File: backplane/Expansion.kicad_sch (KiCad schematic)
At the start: 27 parts, among them U401 74HC245, U402 74HC245, U403 74HC245, U404 74HC245, U405 74HC245, U406 74HC245, U407 ATF22V10C, U408 SY100EL14V

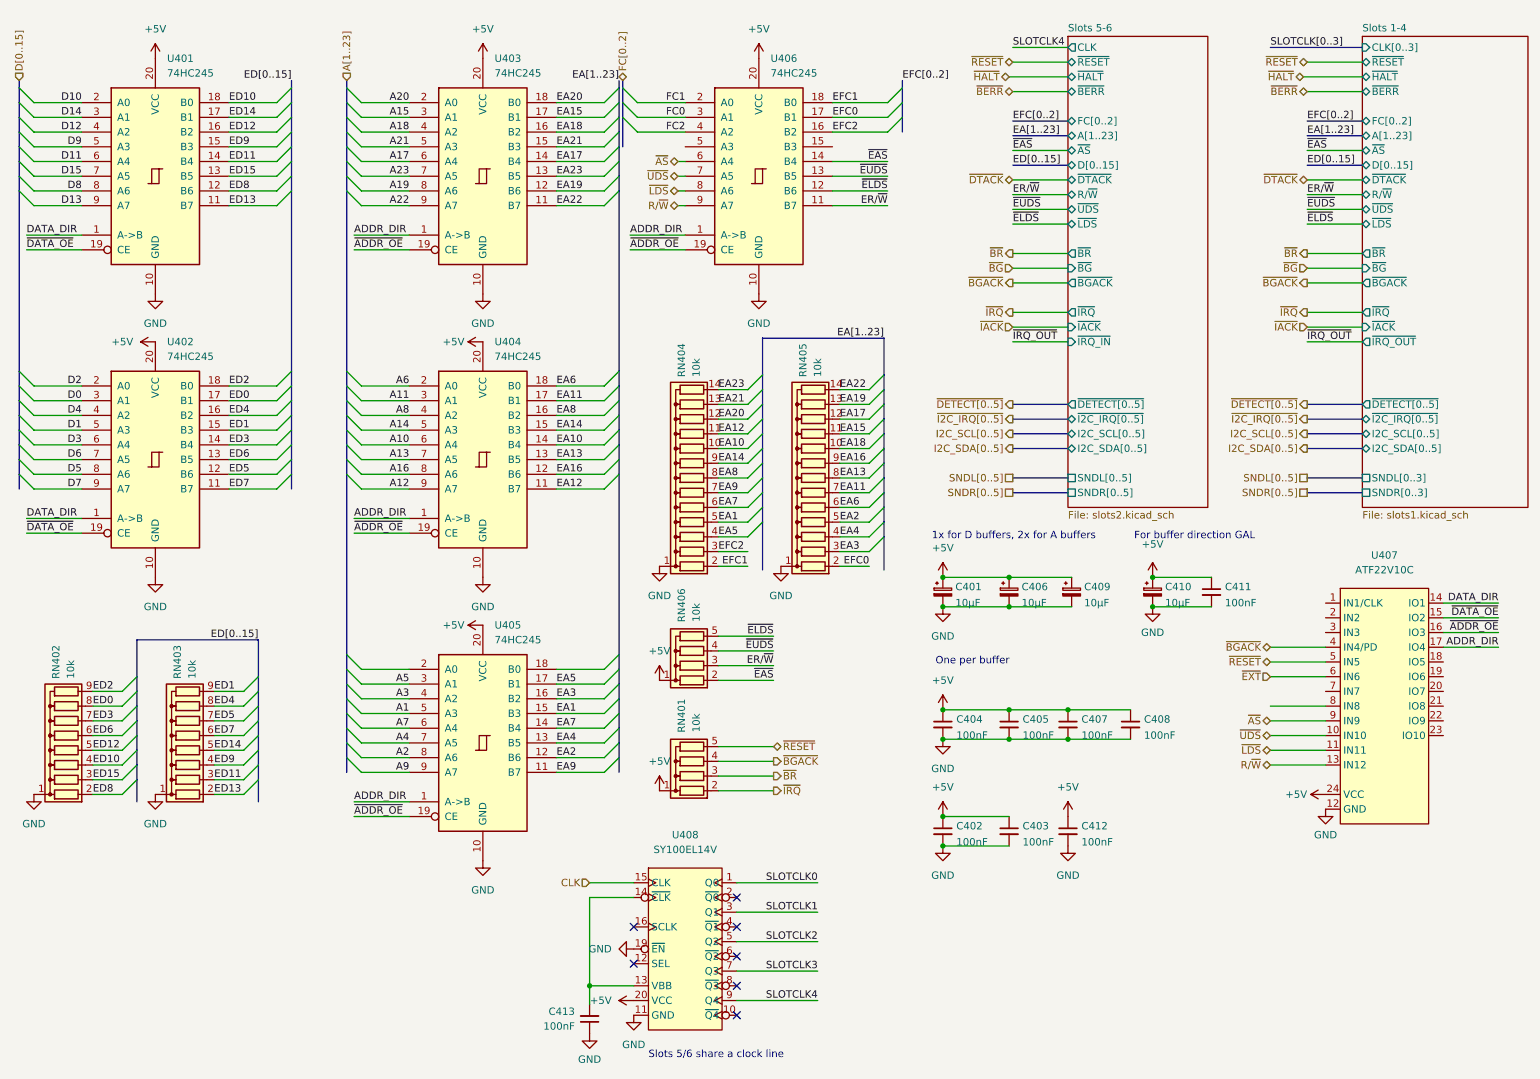
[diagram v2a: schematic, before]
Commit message: Backplane mechanical improvements
- Added screw holes to the backplane; they may or may not actually be
  correct but the spacing between them should be right. We've got holes
  every two HU's (2x .2") for extra spacing/material between holes

- Added reset LED and some more pull ups

- Minor tweaks to backplane management card
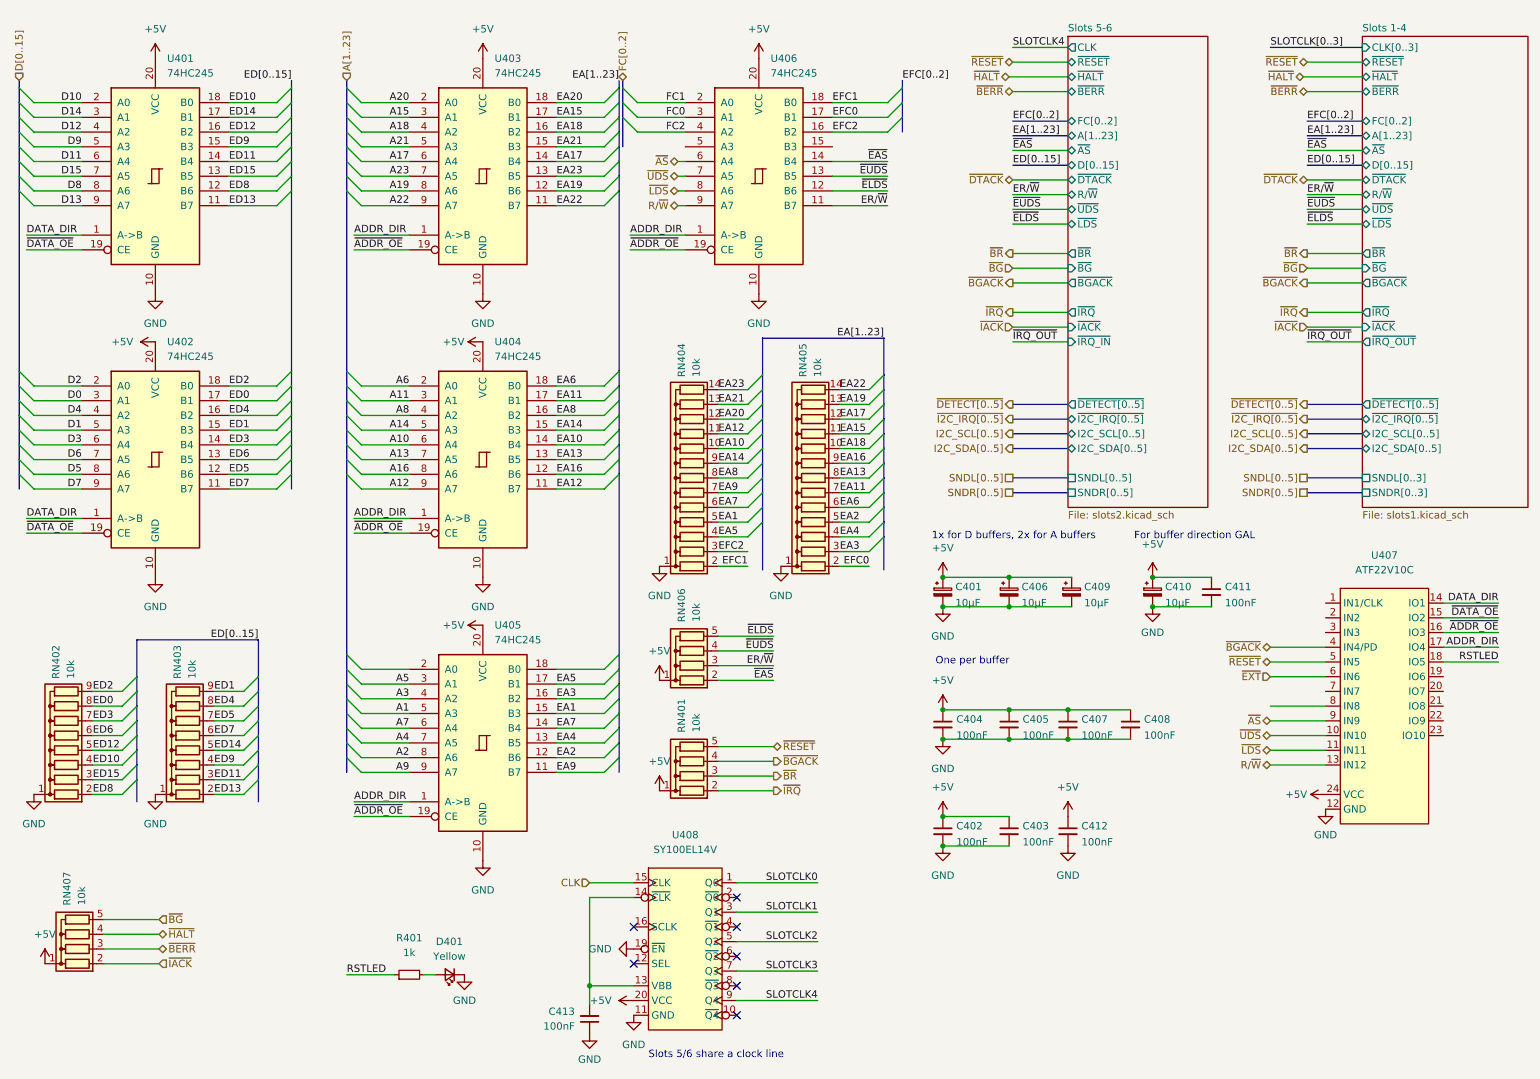
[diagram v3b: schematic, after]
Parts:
- added D401: Yellow, LED_SMD:LED_0805_2012Metric, symbol Device:LED_Small
- added R401: 1k, Resistor_SMD:R_0805_2012Metric, symbol Device:R_Small
- added RN407: 10k, Resistor_THT:R_Array_SIP5, symbol Device:R_Network04
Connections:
- net +5V: now also RN407.1 (common)
- net GND: now also D401.1 (K)
- net ~{BERR}: now also RN407.3 (R2)
- net ~{BG}: now also RN407.5 (R4)
- net ~{HALT}: now also RN407.4 (R3)
- net ~{IACK}: now also RN407.2 (R1)
- net RSTLED: now reaches U407.18 (IO5)
- net RSTLED: now also R401.1
- new net: D401.2 (A), R401.2
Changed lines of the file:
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@@
     (stroke (width 0) (type default) (color 0 0 0 0))
   )
+  (wire (pts (xy 265.43 127) (xy 274.955 127))
+    (stroke (width 0) (type default) (color 0 0 0 0))
+  )
   (wire (pts (xy 120.65 30.48) (xy 112.395 30.48))
     (stroke (width 0) (type default) (color 0 0 0 0))
@@
     (stroke (width 0) (type default) (color 0 0 0 0))
   )
+  (wire (pts (xy 34.29 176.53) (xy 43.815 176.53))
+    (stroke (width 0) (type default) (color 0 0 0 0))
+  )
   (bus (pts (xy 172.085 27.94) (xy 172.085 30.48))
     (stroke (width 0) (type default) (color 0 0 0 0))
@@
     (stroke (width 0) (type default) (color 0 0 0 0))
   )
+  (wire (pts (xy 34.29 179.07) (xy 43.815 179.07))
+    (stroke (width 0) (type default) (color 0 0 0 0))
+  )
   (bus (pts (xy 191.135 36.195) (xy 200.66 36.195))
     (stroke (width 0) (type default) (color 0 0 0 0))
@@
     (stroke (width 0) (type default) (color 0 0 0 0))
   )
+  (wire (pts (xy 34.29 171.45) (xy 43.815 171.45))
+    (stroke (width 0) (type default) (color 0 0 0 0))
+  )
   (bus (pts (xy 241.935 41.275) (xy 251.46 41.275))
     (stroke (width 0) (type default) (color 0 0 0 0))
@@
     (stroke (width 0) (type default) (color 0 0 0 0))
   )
+  (wire (pts (xy 34.29 173.99) (xy 43.815 173.99))
+    (stroke (width 0) (type default) (color 0 0 0 0))
+  )
   (wire (pts (xy 118.11 182.88) (xy 118.11 186.055))
     (stroke (width 0) (type default) (color 0 0 0 0))
@@
     (stroke (width 0) (type default) (color 0 0 0 0))
   )
+  (wire (pts (xy 89.535 180.975) (xy 91.44 180.975))
+    (stroke (width 0) (type default) (color 0 0 0 0))
+  )
   (bus (pts (xy 66.675 35.56) (xy 66.675 38.1))
     (stroke (width 0) (type default) (color 0 0 0 0))
@@
     (stroke (width 0) (type default) (color 0 0 0 0))
   )
+  (wire (pts (xy 84.455 180.975) (xy 76.2 180.975))
+    (stroke (width 0) (type default) (color 0 0 0 0))
+  )
   (bus (pts (xy 147.955 85.09) (xy 147.955 87.63))
     (stroke (width 0) (type default) (color 0 0 0 0))
@@
     (effects (font (size 1.27 1.27)) (justify left bottom))
   )
+  (label "RSTLED" (at 274.955 127 180)
+    (effects (font (size 1.27 1.27)) (justify right bottom))
+  )
   (label "D11" (at 30.48 40.64 180)
     (effects (font (size 1.27 1.27)) (justify right bottom))
@@
     (effects (font (size 1.27 1.27)) (justify right bottom))
   )
+  (label "RSTLED" (at 76.2 180.975 0)
+    (effects (font (size 1.27 1.27)) (justify left bottom))
+  )
   (label "D7" (at 30.48 97.155 180)
     (effects (font (size 1.27 1.27)) (justify right bottom))
@@
     (effects (font (size 1.27 1.27)) (justify right))
   )
+  (hierarchical_label "~{HALT}" (shape bidirectional) (at 43.815 173.99 0)
+    (effects (font (size 1.27 1.27)) (justify left))
+  )
   (hierarchical_label "~{IRQ}" (shape output) (at 241.935 66.675 180)
     (effects (font (size 1.27 1.27)) (justify right))
@@
     (effects (font (size 1.27 1.27)) (justify left))
   )
+  (hierarchical_label "~{IACK}" (shape input) (at 43.815 179.07 0)
+    (effects (font (size 1.27 1.27)) (justify left))
+  )
   (hierarchical_label "~{BG}" (shape input) (at 241.935 59.055 180)
     (effects (font (size 1.27 1.27)) (justify right))
@@
     (effects (font (size 1.27 1.27)) (justify right))
   )
+  (hierarchical_label "~{BG}" (shape input) (at 43.815 171.45 0)
+    (effects (font (size 1.27 1.27)) (justify left))
+  )
   (hierarchical_label "~{DTACK}" (shape bidirectional) (at 241.935 43.815 180)
     (effects (font (size 1.27 1.27)) (justify right))
@@
     (effects (font (size 1.27 1.27)) (justify right))
   )
+  (hierarchical_label "~{BERR}" (shape bidirectional) (at 43.815 176.53 0)
+    (effects (font (size 1.27 1.27)) (justify left))
+  )
   (hierarchical_label "~{RESET}" (shape bidirectional) (at 241.935 23.495 180)
     (effects (font (size 1.27 1.27)) (justify right))
@@
     (pin "2")
   )
+  (symbol (lib_id "Device:R_Network04") (at 29.21 173.99 90) (unit 1)
+    (in_bom yes) (on_board yes)
+    (property "Reference" "RN407" (id 0) (at 27.94 163.195 0)
+      (effects (font (size 1.27 1.27)) (justify right))
+    )
+    (property "Value" "10k" (id 1) (at 30.48 165.735 0)
+      (effects (font (size 1.27 1.27)) (justify right))
+    )
+    (property "Footprint" "Resistor_THT:R_Array_SIP5" (id 2) (at 29.21 167.005 90)
+      (effects (font (size 1.27 1.27)) hide)
+    )
+    (property "Datasheet" "http://www.vishay.com/docs/31509/csc.pdf" (id 3) (at 29.21 173.99 0)
+      (effects (font (size 1.27 1.27)) hide)
+    )
+    (property "MPN" "4605X-101-103LF" (id 4) (at 29.21 173.99 90)
+      (effects (font (size 1.27 1.27)) hide)
+    )
+    (pin "1")
+    (pin "2")
+    (pin "3")
+    (pin "4")
+    (pin "5")
+  )
   (symbol (lib_id "Device:C_Small") (at 190.5 137.795 0) (unit 1)
     (in_bom yes) (on_board yes) (fields_autoplaced)
@@
     (pin "1")
   )
+  (symbol (lib_id "power:+5V") (at 24.13 179.07 0) (unit 1)
+    (in_bom yes) (on_board yes) (fields_autoplaced)
+    (property "Reference" "#PWR0430" (id 0) (at 24.13 182.88 0)
+      (effects (font (size 1.27 1.27)) hide)
+    )
+    (property "Value" "+5V" (id 1) (at 24.13 173.99 0))
+    (property "Footprint" "" (id 2) (at 24.13 179.07 0)
+      (effects (font (size 1.27 1.27)) hide)
+    )
+    (property "Datasheet" "" (id 3) (at 24.13 179.07 0)
+      (effects (font (size 1.27 1.27)) hide)
+    )
+    (pin "1")
+  )
   (symbol (lib_id "power:+5V") (at 125.73 185.42 90) (unit 1)
     (in_bom yes) (on_board yes) (fields_autoplaced)
@@
     (pin "1")
   )
+  (symbol (lib_id "Device:R_Small") (at 86.995 180.975 90) (unit 1)
+    (in_bom yes) (on_board yes) (fields_autoplaced)
+    (property "Reference" "R401" (id 0) (at 86.995 174.625 90))
+    (property "Value" "1k" (id 1) (at 86.995 177.165 90))
+    (property "Footprint" "Resistor_SMD:R_0805_2012Metric" (id 2) (at 86.995 180.975 0)
+      (effects (font (size 1.27 1.27)) hide)
+    )
+    (property "Datasheet" "~" (id 3) (at 86.995 180.975 0)
+      (effects (font (size 1.27 1.27)) hide)
+    )
+    (pin "1")
+    (pin "2")
+  )
+  (symbol (lib_id "power:GND") (at 96.52 180.975 0) (unit 1)
+    (in_bom yes) (on_board yes) (fields_autoplaced)
+    (property "Reference" "#PWR0130" (id 0) (at 96.52 187.325 0)
+      (effects (font (size 1.27 1.27)) hide)
+    )
+    (property "Value" "GND" (id 1) (at 96.52 185.42 0))
+    (property "Footprint" "" (id 2) (at 96.52 180.975 0)
+      (effects (font (size 1.27 1.27)) hide)
+    )
+    (property "Datasheet" "" (id 3) (at 96.52 180.975 0)
+      (effects (font (size 1.27 1.27)) hide)
+    )
+    (pin "1")
+  )
   (symbol (lib_id "74xx:74HC245") (at 147.32 43.18 0) (unit 1)
     (in_bom yes) (on_board yes) (fields_autoplaced)
@@
       (effects (font (size 1.27 1.27)) hide)
     )
+    (pin "1")
+    (pin "2")
+  )
+  (symbol (lib_id "Device:LED_Small") (at 93.98 180.975 180) (unit 1)
+    (in_bom yes) (on_board yes) (fields_autoplaced)
+    (property "Reference" "D401" (id 0) (at 93.9165 175.26 0))
+    (property "Value" "Yellow" (id 1) (at 93.9165 177.8 0))
+    (property "Footprint" "LED_SMD:LED_0805_2012Metric" (id 2) (at 93.98 180.975 90)
+      (effects (font (size 1.27 1.27)) hide)
+    )
+    (property "Datasheet" "~" (id 3) (at 93.98 180.975 90)
+      (effects (font (size 1.27 1.27)) hide)
+    )
+    (property "MPN" "AP2012YD" (id 4) (at 93.98 180.975 0)
+      (effects (font (size 1.27 1.27)) hide)
+    )

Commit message: Minor tweaks to all boards
- Moved around some traces on the 68000 CPU card for prettiness

- Added a connector on the backplane to provide +5V/+12V without a
  management card installed (for testing)
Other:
- company: (none) -> Tristan Seifert
- title: (none) -> Backplane
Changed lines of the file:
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@@
   (paper "A4")
   (title_block
+    (title "Backplane")
+    (date "2022-01-09")
+    (rev "1")
+    (company "Tristan Seifert")
     (comment 1 "Buffers may be substituted with 74VHC245 for higher speed")
   )

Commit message: Minor layout tweaks across the board
- Added an input for a test clock, and a jumper for sending this clock
  instead of the CPU clock to the clock pins of the expansion cards on
  the backplane boards

- Reworked a bunch of the power supply board

- Minor changes (to consolidate BOMs) on CPU board for some capacitors,
  they were replaced with SMD versions
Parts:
- added JP401: Jumper_2_Open, Connector_PinHeader_2.54mm:PinHeader_1x02_P2.54mm_Vertical, symbol Jumper:Jumper_2_Open
- added TP401: ALTCLK, TestPoint:TestPoint_Keystone_5000-5004_Miniature, symbol Connector:TestPoint
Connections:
- net +5V: now also JP401.1 (A)
- net CLKSEL: now reaches U408.12 (SEL)
- net CLKSEL: now also JP401.2 (B)
- net ALTCLK: now reaches U408.16 (SCLK)
- net ALTCLK: now also TP401.1
- no-connect marks 7 -> 5
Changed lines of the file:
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@@
     (company "Tristan Seifert")
     (comment 1 "Buffers may be substituted with 74VHC245 for higher speed")
+    (comment 2 "Close JP401 to send ALTCLK to slot clock pins instead of CPU clk")
   )
   (junction (at 179.07 140.335) (diameter 0) (color 0 0 0 0)
@@
   (no_connect (at 143.51 182.88))
   (no_connect (at 143.51 167.64))
-  (no_connect (at 125.73 179.07))
-  (no_connect (at 125.73 172.72))
   (no_connect (at 143.51 172.72))
   (bus_entry (at 168.91 80.01) (size -2.54 2.54)
@@
     (stroke (width 0) (type default) (color 0 0 0 0))
   )
+  (wire (pts (xy 68.58 187.96) (xy 78.105 187.96))
+    (stroke (width 0) (type default) (color 0 0 0 0))
+  )
   (bus (pts (xy 40.005 132.08) (xy 40.005 134.62))
     (stroke (width 0) (type default) (color 0 0 0 0))
@@
     (stroke (width 0) (type default) (color 0 0 0 0))
   )
+  (wire (pts (xy 118.745 172.72) (xy 125.73 172.72))
+    (stroke (width 0) (type default) (color 0 0 0 0))
+  )
   (bus (pts (xy 147.955 82.55) (xy 147.955 85.09))
     (stroke (width 0) (type default) (color 0 0 0 0))
@@
     (stroke (width 0) (type default) (color 0 0 0 0))
   )
+  (wire (pts (xy 82.55 169.545) (xy 90.805 169.545))
+    (stroke (width 0) (type default) (color 0 0 0 0))
+  )
   (bus (pts (xy 123.19 89.535) (xy 123.19 92.075))
     (stroke (width 0) (type default) (color 0 0 0 0))
@@
     (stroke (width 0) (type default) (color 0 0 0 0))
   )
+  (wire (pts (xy 118.745 179.07) (xy 125.73 179.07))
+    (stroke (width 0) (type default) (color 0 0 0 0))
+  )
   (wire (pts (xy 160.02 30.48) (xy 169.545 30.48))
     (stroke (width 0) (type default) (color 0 0 0 0))
@@
     (effects (font (size 1.27 1.27)) (justify right bottom))
   )
+  (label "ALTCLK" (at 118.745 172.72 0)
+    (effects (font (size 1.27 1.27)) (justify left bottom))
+  )
   (label "~{IRQ_OUT}" (at 191.135 71.755 0)
     (effects (font (size 1.27 1.27)) (justify left bottom))
@@
     (effects (font (size 1.27 1.27)) (justify right bottom))
   )
-  (label "EFC2" (at 140.335 107.95 0)
-    (effects (font (size 1.27 1.27)) (justify left bottom))
+  (label "EFC2" (at 145.415 107.95 180)
+    (effects (font (size 1.27 1.27)) (justify right bottom))
   )
   (label "ED12" (at 55.88 35.56 0)
@@
     (effects (font (size 1.27 1.27)) (justify left bottom))
   )
+  (label "ALTCLK" (at 90.805 169.545 180)
+    (effects (font (size 1.27 1.27)) (justify right bottom))
+  )
   (label "EA22" (at 161.29 80.01 0)
     (effects (font (size 1.27 1.27)) (justify left bottom))
@@
     (effects (font (size 1.27 1.27)) (justify left bottom))
   )
+  (label "CLKSEL" (at 78.105 187.96 180)
+    (effects (font (size 1.27 1.27)) (justify right bottom))
+  )
   (label "D15" (at 30.48 43.18 180)
     (effects (font (size 1.27 1.27)) (justify right bottom))
@@
     (effects (font (size 1.27 1.27)) (justify left bottom))
   )
+  (label "CLKSEL" (at 118.745 179.07 0)
+    (effects (font (size 1.27 1.27)) (justify left bottom))
+  )
   (label "D3" (at 30.48 89.535 180)
     (effects (font (size 1.27 1.27)) (justify right bottom))
@@
     (pin "1")
   )
+  (symbol (lib_id "Jumper:Jumper_2_Open") (at 63.5 187.96 0) (unit 1)
+    (in_bom yes) (on_board yes) (fields_autoplaced)
+    (property "Reference" "JP401" (id 0) (at 63.5 182.3425 0))
+    (property "Value" "Jumper_2_Open" (id 1) (at 63.5 185.1176 0))
+    (property "Footprint" "Connector_PinHeader_2.54mm:PinHeader_1x02_P2.54mm_Vertical" (id 2) (at 63.5 187.96 0)
+      (effects (font (size 1.27 1.27)) hide)
+    )
+    (property "Datasheet" "~" (id 3) (at 63.5 187.96 0)
+      (effects (font (size 1.27 1.27)) hide)
+    )
+    (pin "1")
+    (pin "2")
+  )
   (symbol (lib_id "Device:C_Polarized_Small") (at 215.265 114.935 0) (unit 1)
     (in_bom yes) (on_board yes) (fields_autoplaced)
@@
     (pin "1")
   )
+  (symbol (lib_id "Connector:TestPoint") (at 82.55 169.545 90) (unit 1)
+    (in_bom yes) (on_board yes) (fields_autoplaced)
+    (property "Reference" "TP401" (id 0) (at 79.248 164.9435 90))
+    (property "Value" "ALTCLK" (id 1) (at 79.248 167.7186 90))
+    (property "Footprint" "TestPoint:TestPoint_Keystone_5000-5004_Miniature" (id 2) (at 82.55 164.465 0)
+      (effects (font (size 1.27 1.27)) hide)
+    )
+    (property "Datasheet" "~" (id 3) (at 82.55 164.465 0)
+      (effects (font (size 1.27 1.27)) hide)
+    )
+    (pin "1")
+  )
   (symbol (lib_id "68komputer-common:SY100EL14V") (at 134.62 162.56 0) (unit 1)
     (in_bom yes) (on_board yes) (fields_autoplaced)
@@
     (pin "2")
   )
+  (symbol (lib_id "power:+5V") (at 58.42 187.96 90) (unit 1)
+    (in_bom yes) (on_board yes) (fields_autoplaced)
+    (property "Reference" "#PWR0431" (id 0) (at 62.23 187.96 0)
+      (effects (font (size 1.27 1.27)) hide)
+    )
+    (property "Value" "+5V" (id 1) (at 55.2451 188.439 90)
+      (effects (font (size 1.27 1.27)) (justify left))
+    )
+    (property "Footprint" "" (id 2) (at 58.42 187.96 0)
+      (effects (font (size 1.27 1.27)) hide)
+    )
+    (property "Datasheet" "" (id 3) (at 58.42 187.96 0)
+      (effects (font (size 1.27 1.27)) hide)
+    )
+    (pin "1")
+  )
   (symbol (lib_id "Device:C_Polarized_Small") (at 201.295 114.935 0) (unit 1)
